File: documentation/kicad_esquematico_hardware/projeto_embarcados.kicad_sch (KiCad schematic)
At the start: 6 parts, among them M1 Motor_Servo, M2 Motor_Servo, Q1 IRLZ44N, Q2 IRLZ44N, U1 ESP32-WROOM-32, U2 MPU-6050

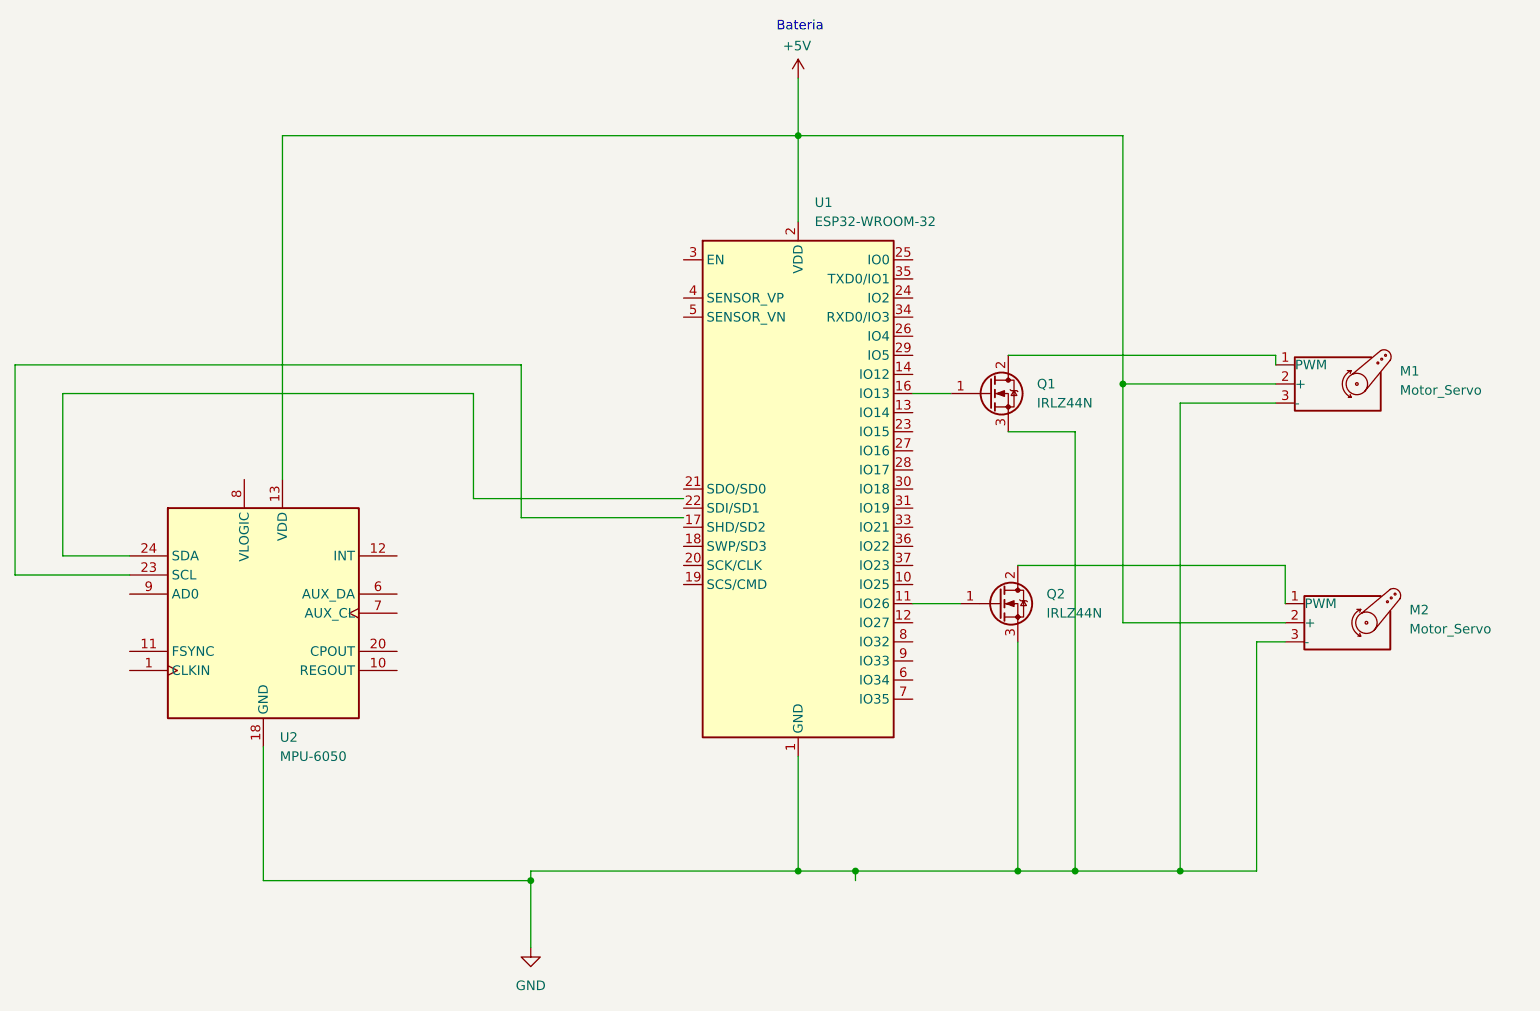
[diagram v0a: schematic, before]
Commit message: fix: gpios servos
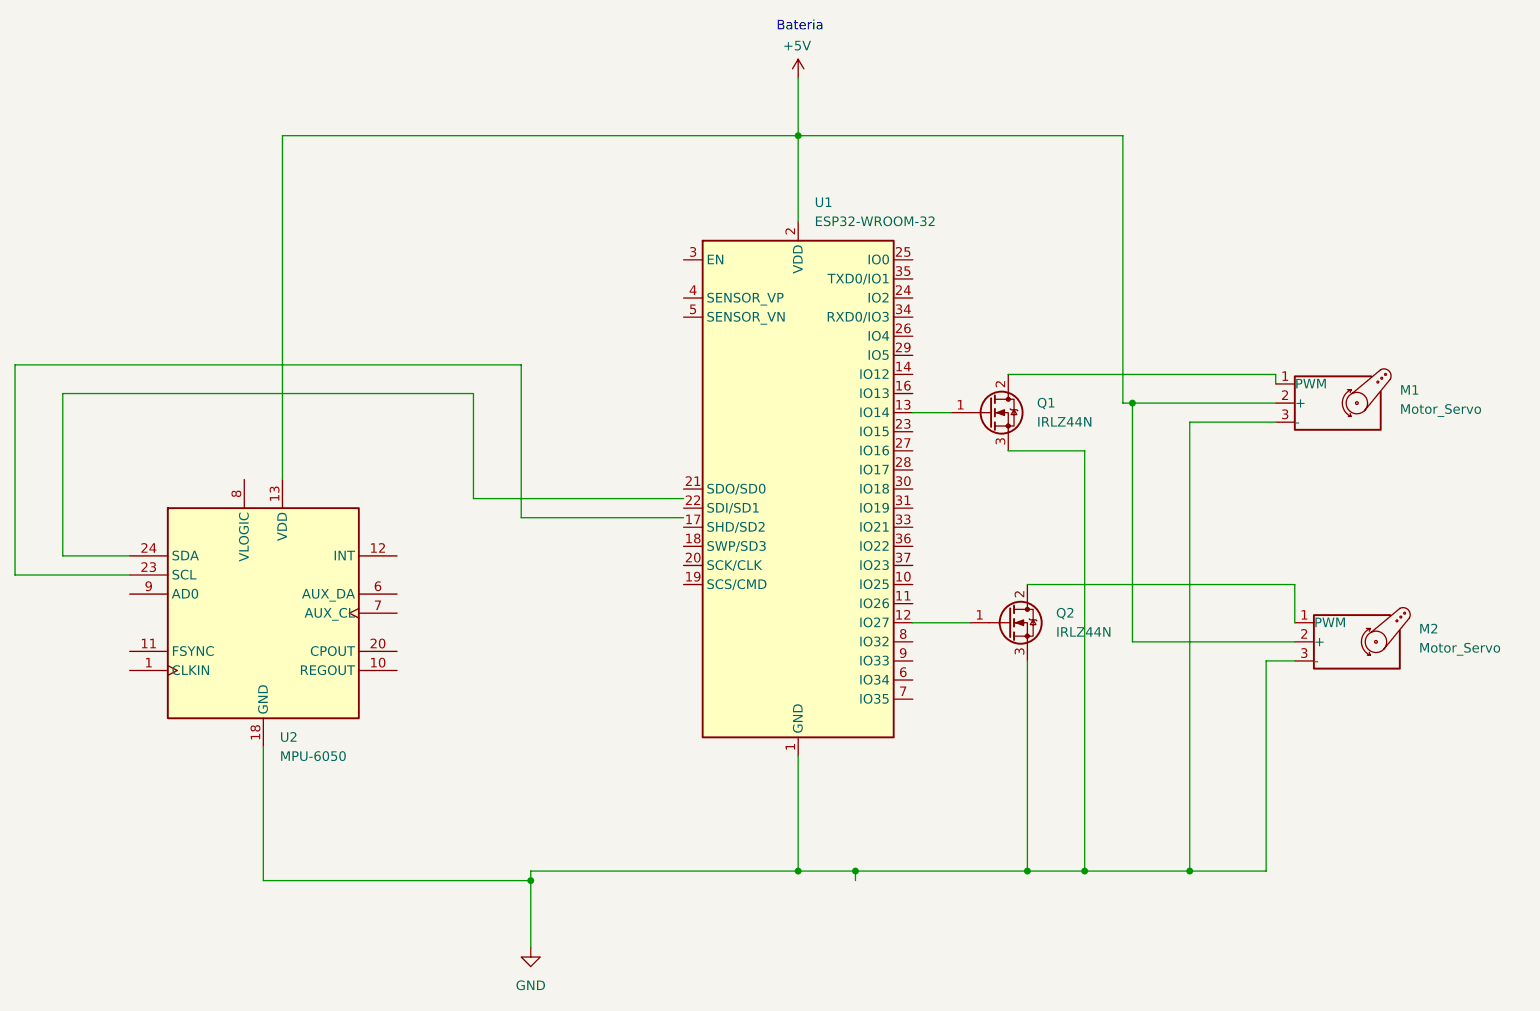
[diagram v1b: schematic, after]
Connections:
- net at Q2.1 (G): now also U1.12 (IO27); no longer U1.11 (IO26)
- net at Q1.1 (G): now also U1.13 (IO14); no longer U1.16 (IO13)
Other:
- moved on the sheet: M1, M2, Q1, Q2

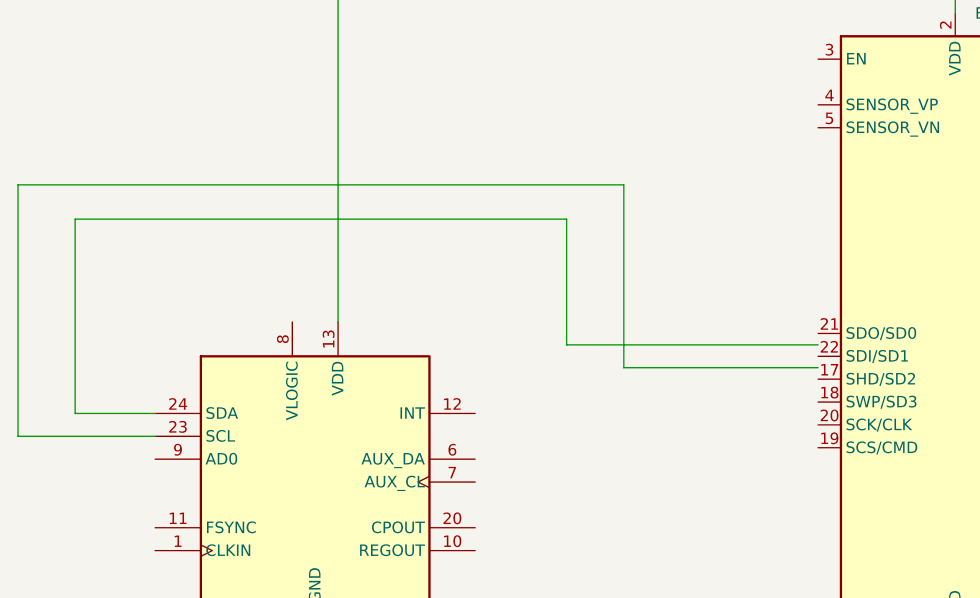
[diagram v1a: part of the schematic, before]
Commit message: fix: gpios servos
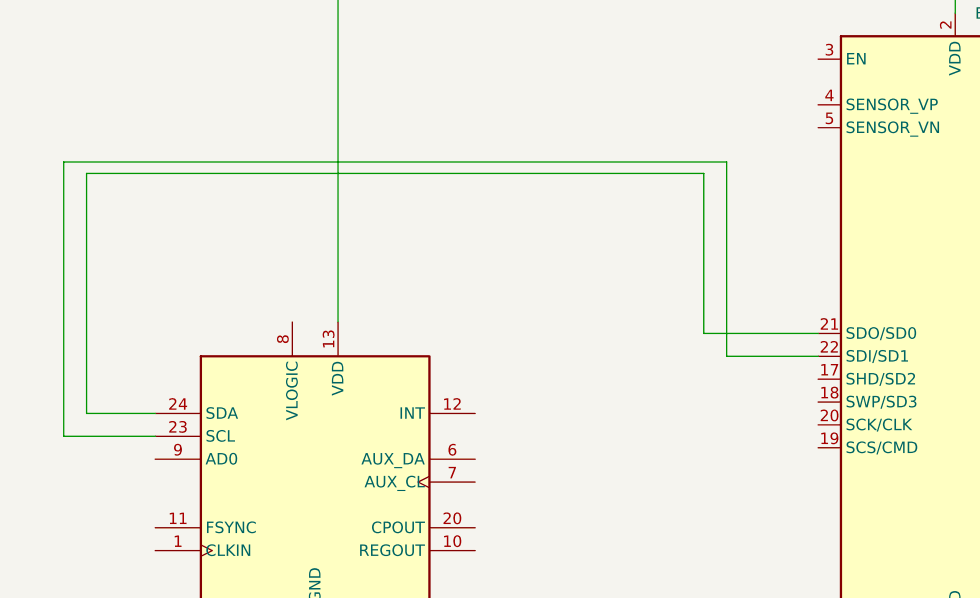
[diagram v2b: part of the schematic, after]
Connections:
- net at U2.23 (SCL): now also U1.22 (SDI/SD1)
- net at U2.24 (SDA): now also U1.21 (SDO/SD0)
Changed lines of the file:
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@@
-	(wire
-		(pts
-			(xy 63.5 78.74) (xy 63.5 100.33)
-		)
-		(stroke
-			(width 0)
-			(type default)
-			(color 26 39 255 1)
-		)
-	)
-	(wire
-		(pts
-			(xy 63.5 78.74) (xy 118.11 78.74)
-		)
-		(stroke
-			(width 0)
-			(type default)
-			(color 26 39 255 1)
-		)
-	)
 	(wire
 		(pts
@@
 	(wire
 		(pts
+			(xy 133.35 73.66) (xy 133.35 91.44)
+		)
+		(stroke
+			(width 0)
+			(type default)
+			(color 0 15 255 1)
+		)
+	)
+	(wire
+		(pts
 			(xy 161.29 44.45) (xy 204.47 44.45)
 		)
@@
 	(wire
 		(pts
-			(xy 124.46 95.25) (xy 146.05 95.25)
-		)
-		(stroke
-			(width 0)
-			(type default)
-			(color 255 0 235 1)
+			(xy 64.77 100.33) (xy 64.77 73.66)
+		)
+		(stroke
+			(width 0)
+			(type default)
+			(color 0 36 255 1)
 		)
 	)
@@
 	(wire
 		(pts
-			(xy 63.5 100.33) (xy 72.39 100.33)
-		)
-		(stroke
-			(width 0)
-			(type default)
-			(color 26 39 255 1)
-		)
-	)
-	(wire
-		(pts
 			(xy 161.29 44.45) (xy 161.29 55.88)
 		)
@@
 	(wire
 		(pts
-			(xy 57.15 102.87) (xy 57.15 74.93)
-		)
-		(stroke
-			(width 0)
-			(type default)
-			(color 255 0 235 1)
-		)
-	)
-	(wire
-		(pts
 			(xy 161.29 44.45) (xy 161.29 36.83)
 		)
@@
 	(wire
 		(pts
+			(xy 135.89 72.39) (xy 135.89 93.98)
+		)
+		(stroke
+			(width 0)
+			(type default)
+			(color 243 0 255 1)
+		)
+	)
+	(wire
+		(pts
 			(xy 161.29 142.24) (xy 125.73 142.24)
 		)
@@
 	(wire
 		(pts
-			(xy 57.15 74.93) (xy 124.46 74.93)
-		)
-		(stroke
-			(width 0)
-			(type default)
-			(color 255 0 235 1)
-		)
-	)
-	(wire
-		(pts
-			(xy 57.15 102.87) (xy 72.39 102.87)
-		)
-		(stroke
-			(width 0)
-			(type default)
-			(color 255 0 235 1)
-		)
-	)
-	(wire
-		(pts
 			(xy 205.74 80.01) (xy 205.74 111.76)
 		)
@@
 	(wire
 		(pts
-			(xy 118.11 92.71) (xy 146.05 92.71)
-		)
-		(stroke
-			(width 0)
-			(type default)
-			(color 26 39 255 1)
-		)
-	)
-	(wire
-		(pts
-			(xy 124.46 74.93) (xy 124.46 95.25)
-		)
-		(stroke
-			(width 0)
-			(type default)
-			(color 255 0 235 1)
+			(xy 135.89 93.98) (xy 146.05 93.98)
+		)
+		(stroke
+			(width 0)
+			(type default)
+			(color 243 0 255 1)
 		)
 	)
@@
 	(wire
 		(pts
+			(xy 72.39 100.33) (xy 64.77 100.33)
+		)
+		(stroke
+			(width 0)
+			(type default)
+			(color 0 36 255 1)
+		)
+	)
+	(wire
+		(pts
 			(xy 227.33 104.14) (xy 227.33 109.22)
 		)
@@
 	(wire
 		(pts
+			(xy 72.39 102.87) (xy 62.23 102.87)
+		)
+		(stroke
+			(width 0)
+			(type default)
+			(color 243 0 255 1)
+		)
+	)
+	(wire
+		(pts
 			(xy 223.52 114.3) (xy 223.52 142.24)
 		)
@@
 	(wire
 		(pts
-			(xy 118.11 78.74) (xy 118.11 92.71)
-		)
-		(stroke
-			(width 0)
-			(type default)
-			(color 26 39 255 1)
-		)
-	)
-	(wire
-		(pts
 			(xy 191.77 114.3) (xy 191.77 142.24)
 		)
@@
 	(wire
 		(pts
+			(xy 62.23 72.39) (xy 135.89 72.39)
+		)
+		(stroke
+			(width 0)
+			(type default)
+			(color 243 0 255 1)
+		)
+	)
+	(wire
+		(pts
 			(xy 213.36 82.55) (xy 213.36 142.24)
 		)
@@
 		)
 	)
+	(wire
+		(pts
+			(xy 64.77 73.66) (xy 133.35 73.66)
+		)
+		(stroke
+			(width 0)
+			(type default)
+			(color 0 36 255 1)
+		)
+	)
+	(wire
+		(pts
+			(xy 133.35 91.44) (xy 146.05 91.44)
+		)
+		(stroke
+			(width 0)
+			(type default)
+			(color 0 88 255 1)
+		)
+	)
+	(wire
+		(pts
+			(xy 62.23 102.87) (xy 62.23 72.39)
+		)
+		(stroke
+			(width 0)
+			(type default)
+			(color 243 0 255 1)
+		)
+	)
